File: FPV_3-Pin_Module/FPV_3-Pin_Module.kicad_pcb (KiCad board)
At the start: 2 copper layers, 33.5 x 25.2 mm, 4 parts, among them J1 Conn_01x10_Socket, J2 Conn_01x03_Socket, J3 Conn_01x10_Socket

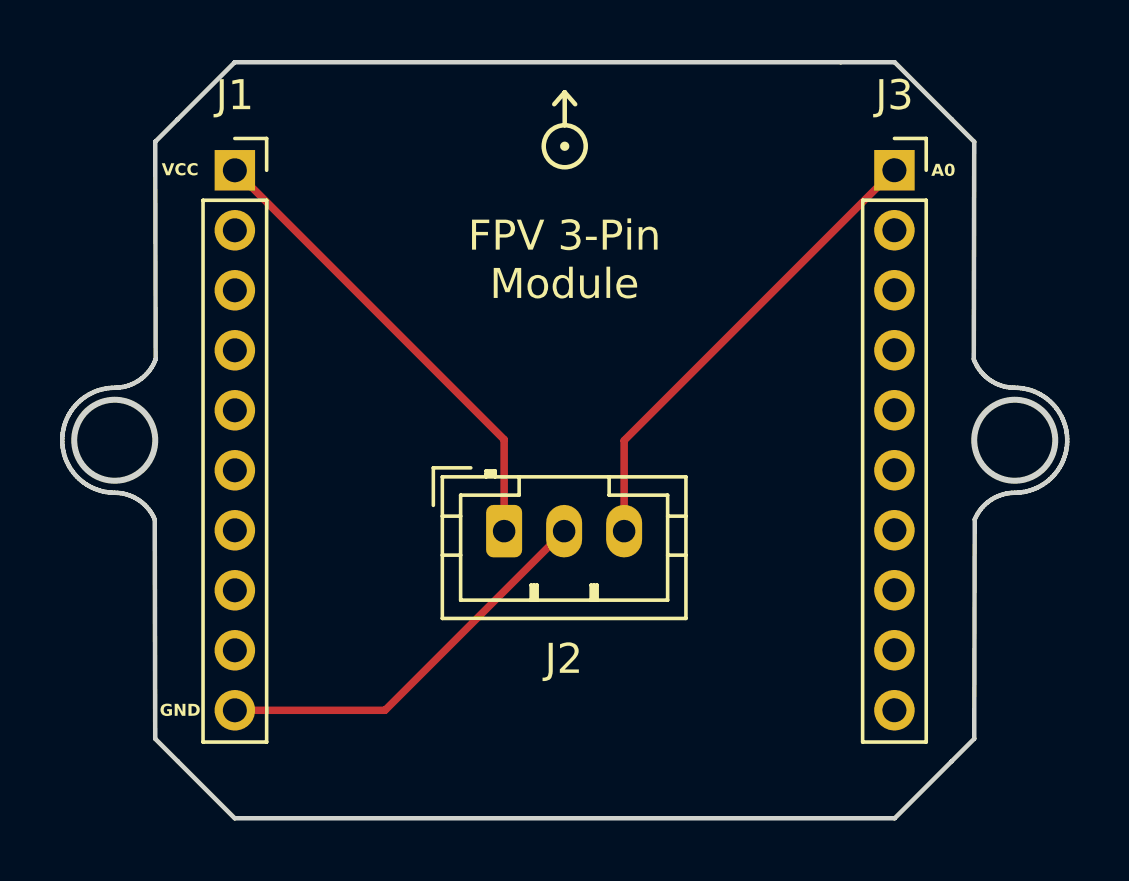
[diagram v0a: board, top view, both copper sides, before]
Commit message: Adding FPV 4-pin interface module
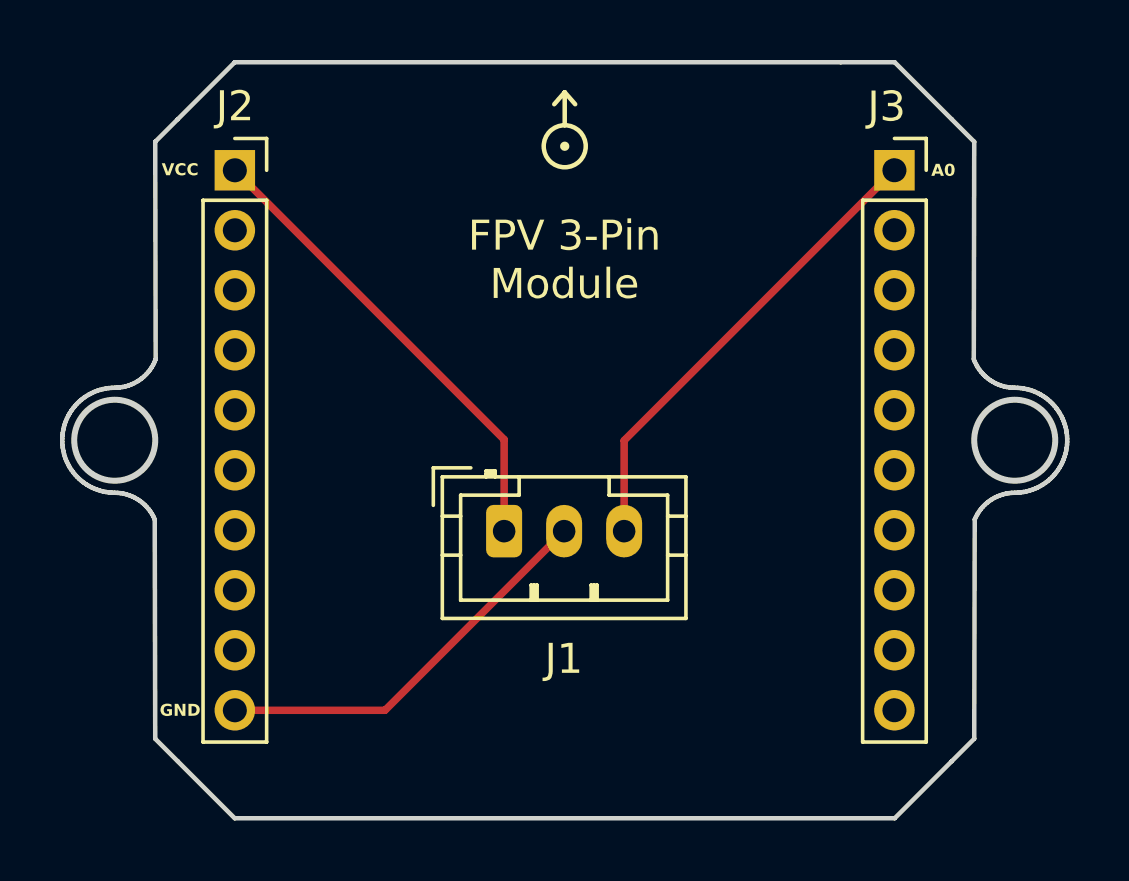
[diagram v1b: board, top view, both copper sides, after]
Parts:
- renumbered J2 to J1, J1 to J2
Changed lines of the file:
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@@
   (net 0 "")
   (net 1 "Net-(J1-Pin_1)")
-  (net 2 "unconnected-(J1-Pin_2-Pad2)")
-  (net 3 "unconnected-(J1-Pin_3-Pad3)")
-  (net 4 "unconnected-(J1-Pin_4-Pad4)")
-  (net 5 "unconnected-(J1-Pin_5-Pad5)")
-  (net 6 "unconnected-(J1-Pin_6-Pad6)")
-  (net 7 "unconnected-(J1-Pin_7-Pad7)")
-  (net 8 "unconnected-(J1-Pin_8-Pad8)")
-  (net 9 "unconnected-(J1-Pin_9-Pad9)")
-  (net 10 "Net-(J1-Pin_10)")
-  (net 11 "Net-(J2-Pin_3)")
+  (net 2 "Net-(J1-Pin_2)")
+  (net 3 "Net-(J1-Pin_3)")
+  (net 4 "unconnected-(J2-Pin_2-Pad2)")
+  (net 5 "unconnected-(J2-Pin_3-Pad3)")
+  (net 6 "unconnected-(J2-Pin_4-Pad4)")
+  (net 7 "unconnected-(J2-Pin_5-Pad5)")
+  (net 8 "unconnected-(J2-Pin_6-Pad6)")
+  (net 9 "unconnected-(J2-Pin_7-Pad7)")
+  (net 10 "unconnected-(J2-Pin_8-Pad8)")
+  (net 11 "unconnected-(J2-Pin_9-Pad9)")
   (net 12 "unconnected-(J3-Pin_2-Pad2)")
   (net 13 "unconnected-(J3-Pin_3-Pad3)")
@@
     (property "ki_keywords" "connector")
     (attr through_hole)
-    (fp_text reference "J2" (at 1.99 4.26) (layer "F.SilkS")
+    (fp_text reference "J1" (at 1.99 4.26) (layer "F.SilkS")
         (effects (font (size 1 1) (thickness 0.15)))
     )
@@
       (net 1 "Net-(J1-Pin_1)") (pinfunction "Pin_1") (pintype "passive"))
     (pad "2" thru_hole oval (at 2 0) (size 1.2 1.75) (drill 0.75) (layers "*.Cu" "*.Mask")
-      (net 10 "Net-(J1-Pin_10)") (pinfunction "Pin_2") (pintype "passive"))
+      (net 2 "Net-(J1-Pin_2)") (pinfunction "Pin_2") (pintype "passive"))
     (pad "3" thru_hole oval (at 4 0) (size 1.2 1.75) (drill 0.75) (layers "*.Cu" "*.Mask")
-      (net 11 "Net-(J2-Pin_3)") (pinfunction "Pin_3") (pintype "passive"))
+      (net 3 "Net-(J1-Pin_3)") (pinfunction "Pin_3") (pintype "passive"))
     (model "${KICAD6_3DMODEL_DIR}/Connector_JST.3dshapes/JST_PH_B3B-PH-K_1x03_P2.00mm_Vertical.wrl"
       (offset (xyz 0 0 0))
@@
     (property "ki_keywords" "connector")
     (attr through_hole)
-    (fp_text reference "J1" (at 0 -2.5) (layer "F.SilkS")
+    (fp_text reference "J2" (at 0.0062 -2.131) (layer "F.SilkS")
         (effects (font (size 1 1) (thickness 0.15)))
     )
@@
       (net 1 "Net-(J1-Pin_1)") (pinfunction "Pin_1") (pintype "passive"))
     (pad "2" thru_hole oval (at 0 2) (size 1.35 1.35) (drill 0.8) (layers "*.Cu" "*.Mask")
-      (net 2 "unconnected-(J1-Pin_2-Pad2)") (pinfunction "Pin_2") (pintype "passive+no_connect"))
+      (net 4 "unconnected-(J2-Pin_2-Pad2)") (pinfunction "Pin_2") (pintype "passive+no_connect"))
     (pad "3" thru_hole oval (at 0 4) (size 1.35 1.35) (drill 0.8) (layers "*.Cu" "*.Mask")
-      (net 3 "unconnected-(J1-Pin_3-Pad3)") (pinfunction "Pin_3") (pintype "passive+no_connect"))
+      (net 5 "unconnected-(J2-Pin_3-Pad3)") (pinfunction "Pin_3") (pintype "passive+no_connect"))
     (pad "4" thru_hole oval (at 0 6) (size 1.35 1.35) (drill 0.8) (layers "*.Cu" "*.Mask")
-      (net 4 "unconnected-(J1-Pin_4-Pad4)") (pinfunction "Pin_4") (pintype "passive+no_connect"))
+      (net 6 "unconnected-(J2-Pin_4-Pad4)") (pinfunction "Pin_4") (pintype "passive+no_connect"))
     (pad "5" thru_hole oval (at 0 8) (size 1.35 1.35) (drill 0.8) (layers "*.Cu" "*.Mask")
-      (net 5 "unconnected-(J1-Pin_5-Pad5)") (pinfunction "Pin_5") (pintype "passive+no_connect"))
+      (net 7 "unconnected-(J2-Pin_5-Pad5)") (pinfunction "Pin_5") (pintype "passive+no_connect"))
     (pad "6" thru_hole oval (at 0 10) (size 1.35 1.35) (drill 0.8) (layers "*.Cu" "*.Mask")
-      (net 6 "unconnected-(J1-Pin_6-Pad6)") (pinfunction "Pin_6") (pintype "passive+no_connect"))
+      (net 8 "unconnected-(J2-Pin_6-Pad6)") (pinfunction "Pin_6") (pintype "passive+no_connect"))
     (pad "7" thru_hole oval (at 0 12) (size 1.35 1.35) (drill 0.8) (layers "*.Cu" "*.Mask")
-      (net 7 "unconnected-(J1-Pin_7-Pad7)") (pinfunction "Pin_7") (pintype "passive+no_connect"))
+      (net 9 "unconnected-(J2-Pin_7-Pad7)") (pinfunction "Pin_7") (pintype "passive+no_connect"))
     (pad "8" thru_hole oval (at 0 14) (size 1.35 1.35) (drill 0.8) (layers "*.Cu" "*.Mask")
-      (net 8 "unconnected-(J1-Pin_8-Pad8)") (pinfunction "Pin_8") (pintype "passive+no_connect"))
+      (net 10 "unconnected-(J2-Pin_8-Pad8)") (pinfunction "Pin_8") (pintype "passive+no_connect"))
     (pad "9" thru_hole oval (at 0 16) (size 1.35 1.35) (drill 0.8) (layers "*.Cu" "*.Mask")
-      (net 9 "unconnected-(J1-Pin_9-Pad9)") (pinfunction "Pin_9") (pintype "passive+no_connect"))
+      (net 11 "unconnected-(J2-Pin_9-Pad9)") (pinfunction "Pin_9") (pintype "passive+no_connect"))
     (pad "10" thru_hole oval (at 0 18) (size 1.35 1.35) (drill 0.8) (layers "*.Cu" "*.Mask")
-      (net 10 "Net-(J1-Pin_10)") (pinfunction "Pin_10") (pintype "passive"))
+      (net 2 "Net-(J1-Pin_2)") (pinfunction "Pin_10") (pintype "passive"))
     (model "${KICAD6_3DMODEL_DIR}/Connector_PinSocket_2.00mm.3dshapes/PinSocket_1x10_P2.00mm_Vertical.wrl"
       (offset (xyz 0 0 0))
@@
     (property "ki_keywords" "connector")
     (attr through_hole)
-    (fp_text reference "J3" (at 0 -2.5) (layer "F.SilkS")
+    (fp_text reference "J3" (at -0.26 -2.12) (layer "F.SilkS")
         (effects (font (size 1 1) (thickness 0.15)))
     )
@@
       (stroke (width 0.1) (type solid)) (layer "F.Fab"))
     (pad "1" thru_hole rect (at 0 0) (size 1.35 1.35) (drill 0.8) (layers "*.Cu" "*.Mask")
-      (net 11 "Net-(J2-Pin_3)") (pinfunction "Pin_1") (pintype "passive"))
+      (net 3 "Net-(J1-Pin_3)") (pinfunction "Pin_1") (pintype "passive"))
     (pad "2" thru_hole oval (at 0 2) (size 1.35 1.35) (drill 0.8) (layers "*.Cu" "*.Mask")
       (net 12 "unconnected-(J3-Pin_2-Pad2)") (pinfunction "Pin_2") (pintype "passive+no_connect"))
@@
   (segment (start 139.55 91.1072) (end 130.5738 82.131) (width 0.25) (layer "F.Cu") (net 1))
   (segment (start 139.55 94.16) (end 139.55 91.1072) (width 0.25) (layer "F.Cu") (net 1))
-  (segment (start 141.55 94.16) (end 135.579 100.131) (width 0.25) (layer "F.Cu") (net 10))
-  (segment (start 135.579 100.131) (end 130.5738 100.131) (width 0.25) (layer "F.Cu") (net 10))
-  (segment (start 143.55 94.16) (end 143.55 91.14) (width 0.25) (layer "F.Cu") (net 11))
-  (segment (start 143.55 91.14) (end 152.56 82.13) (width 0.25) (layer "F.Cu") (net 11))
+  (segment (start 141.55 94.16) (end 135.579 100.131) (width 0.25) (layer "F.Cu") (net 2))
+  (segment (start 135.579 100.131) (end 130.5738 100.131) (width 0.25) (layer "F.Cu") (net 2))
+  (segment (start 143.55 94.16) (end 143.55 91.14) (width 0.25) (layer "F.Cu") (net 3))
+  (segment (start 143.55 91.14) (end 152.56 82.13) (width 0.25) (layer "F.Cu") (net 3))
 )
